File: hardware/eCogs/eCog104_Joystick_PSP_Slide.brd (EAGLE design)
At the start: 47.5 x 28 mm, 6 parts

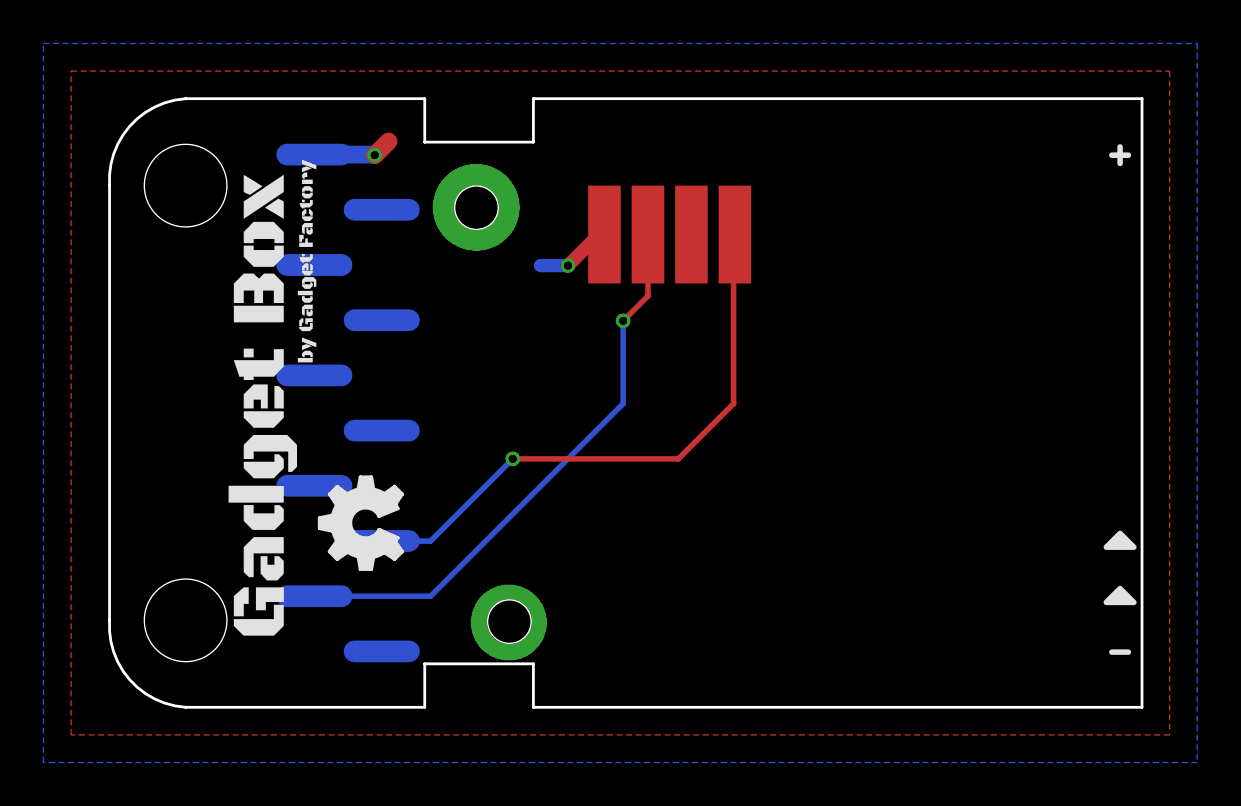
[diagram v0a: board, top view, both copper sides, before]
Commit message: Update eCogs to through hole
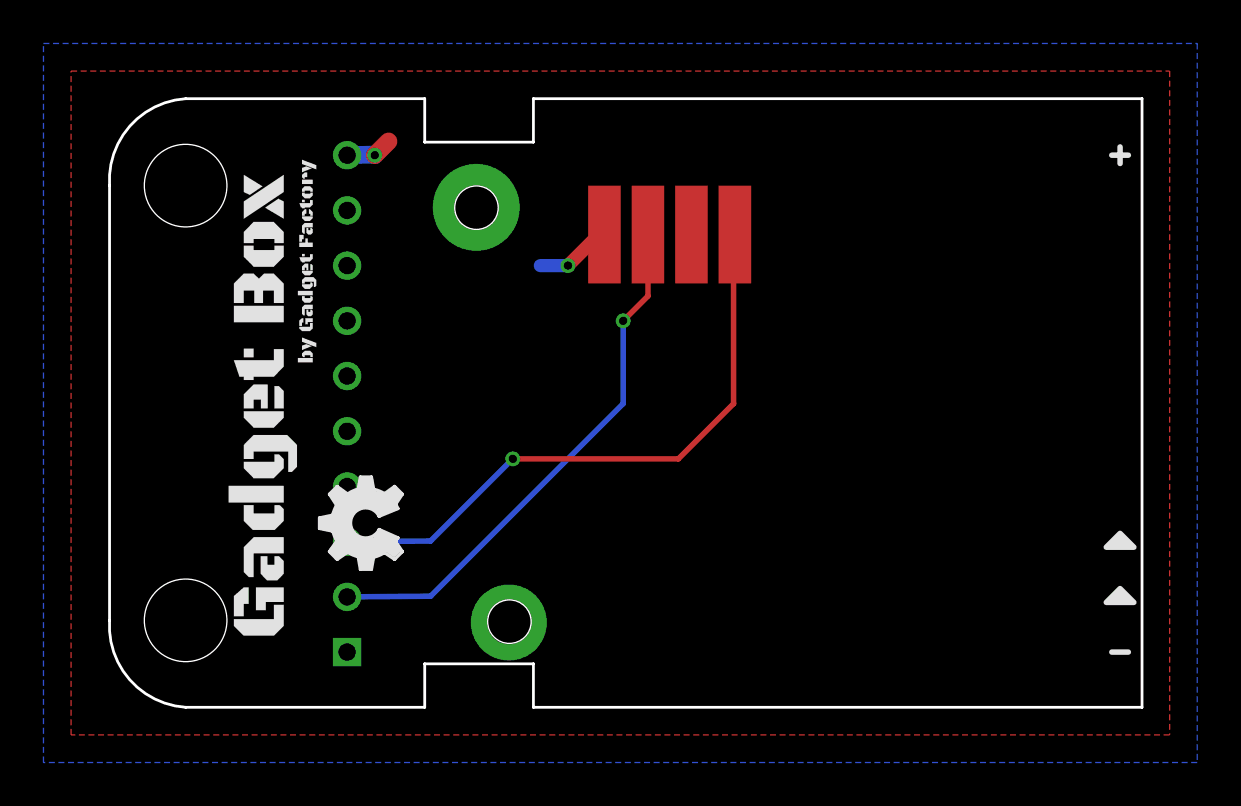
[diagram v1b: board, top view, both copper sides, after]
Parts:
- ECOG: value ECOG_GENERAL_ROWECOG_GENERAL_SMD -> ECOG_GENERAL_ROWTHROUGHOLE; device eCogs:ECOG_GENERAL_SMD -> eCogs:ECOG_GENERAL_TH
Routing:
- net HORIZONTAL: track 26.6 -> 28.2 mm
- net VERTICAL: track 26.1 -> 24.6 mm
- net 3V3: track 3.69 -> 2.18 mm
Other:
- board text added: "ecog104 v2.1"
- board text removed: "ecog104 v2.0"
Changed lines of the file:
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@@
 <plain>
 <text x="45.441" y="17.415" size="0.8128" layer="22" font="vector" rot="MR0">ecog104.GadgetFactory.net</text>
-<text x="39.298" y="1.159" size="1.016" layer="22" font="vector" rot="MR0">ecog104 v2.0</text>
+<text x="39.298" y="1.159" size="1.016" layer="22" font="vector" rot="MR0">ecog104 v2.1</text>
 <text x="39.298" y="2.429" size="1.016" layer="22" font="vector" rot="MR0">PSP Thumb Joystick</text>
 <text x="39.298" y="4.199" size="1.016" layer="22" font="vector" rot="MR0">eCogs</text>
@@
 </autorouter>
 <elements>
-<element name="ECOG" library="eCogs" package="ECOG_GENERAL_SMD" value="ECOG_GENERAL_ROWECOG_GENERAL_SMD" x="0" y="0" smashed="yes">
-<attribute name="DIGIKEY" value="S1013EC-10-ND" x="0" y="0" size="1.778" layer="27" display="off"/>
-</element>
+<element name="ECOG" library="eCogs" package="ECOG_GENERAL_TH" value="ECOG_GENERAL_ROWTHROUGHOLE" x="0" y="0" smashed="yes"/>
 <element name="U$1" library="eCogs" package="LEGEND_ANALOG" value="" x="46.99" y="5.08"/>
 <element name="U$2" library="eCogs" package="LEGEND_ANALOG" value="" x="46.99" y="7.62"/>
@@
 <contactref element="ECOG" pad="3V3"/>
 <contactref element="U$4" pad="VCC"/>
-<wire x1="9.92324375" y1="25.429" x2="12.671" y2="25.429" width="0.8128" layer="16"/>
+<wire x1="11.43" y1="25.4" x2="12.671" y2="25.429" width="0.8128" layer="16"/>
 <wire x1="12.671" y1="25.429" x2="12.7" y2="25.4" width="0.8128" layer="16"/>
 <via x="12.7" y="25.4" extent="1-16" drill="0.381"/>
@@
 <contactref element="U$4" pad="X"/>
 <contactref element="ECOG" pad="G1"/>
-<wire x1="13.02204375" y1="7.649" x2="15.269" y2="7.649" width="0.254" layer="16"/>
+<wire x1="11.43" y1="7.62" x2="15.269" y2="7.649" width="0.254" layer="16"/>
 <wire x1="15.269" y1="7.649" x2="19.05" y2="11.43" width="0.254" layer="16"/>
 <via x="19.05" y="11.43" extent="1-16" drill="0.381"/>
@@
 <contactref element="U$4" pad="Y"/>
 <contactref element="ECOG" pad="G0"/>
-<wire x1="9.92324375" y1="5.1110625" x2="15.2710625" y2="5.1110625" width="0.254" layer="16"/>
+<wire x1="11.43" y1="5.08" x2="15.2710625" y2="5.1110625" width="0.254" layer="16"/>
 <wire x1="15.2710625" y1="5.1110625" x2="24.13" y2="13.97" width="0.254" layer="16"/>
 <wire x1="25.27" y1="21.75" x2="25.27" y2="18.92" width="0.254" layer="1"/>
